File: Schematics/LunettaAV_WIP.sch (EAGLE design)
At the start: 97 parts, among them IC1 7809\, IC10 4051N, IC2 7805, IC3 4040N, IC4 TLC339P, IC5 4046N, IC6 4094N, IC7 40106N, IC8 4046N, IC9 4017N, J1 POWER_JACKPOWER_JACK_SLOT, J3 WQP-PJ301M-12_JACK, U1 LM358, U2 LM358, U3 MICROCHIP_MCP41050-I-PMICROCH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

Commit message: add more caps no cap
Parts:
- added C25: 10uF, SparkFun-Capacitors:10UF-POLAR-RADIAL-2.5MM-25V-20%
- added C26: 0.1uF, SparkFun-Capacitors:0.1UF-KIT-EZ-50V-20%
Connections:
- net 5V: now also C25.+, C26.1
- net GND: now also C25.-, C26.2
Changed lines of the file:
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@@
 <part name="C24" library="SparkFun-Capacitors" deviceset="10UF-POLAR" device="-RADIAL-2.5MM-25V-20%" value="10uF"/>
 <part name="D2" library="diode" library_urn="urn:adsk.eagle:library:210" deviceset="BAT42" device="" package3d_urn="urn:adsk.eagle:package:43344/2"/>
+<part name="C25" library="SparkFun-Capacitors" deviceset="10UF-POLAR" device="-RADIAL-2.5MM-25V-20%" value="10uF"/>
+<part name="C26" library="SparkFun-Capacitors" deviceset="0.1UF" device="-KIT-EZ-50V-20%" value="0.1uF"/>
 </parts>
 <sheets>
@@
 <attribute name="VALUE" x="298.069" y="-103.886" size="1.778" layer="96" rot="R90"/>
 </instance>
+<instance part="C25" gate="G$1" x="132.08" y="-294.64" smashed="yes">
+<attribute name="NAME" x="133.096" y="-294.005" size="1.778" layer="95" font="vector"/>
+<attribute name="VALUE" x="133.096" y="-298.831" size="1.778" layer="96" font="vector"/>
+</instance>
+<instance part="C26" gate="G$1" x="152.4" y="-302.26" smashed="yes">
+<attribute name="NAME" x="153.924" y="-299.339" size="1.778" layer="95" font="vector"/>
+<attribute name="VALUE" x="153.924" y="-304.419" size="1.778" layer="96" font="vector"/>
+</instance>
 </instances>
 <busses>
@@
 <label x="294.64" y="-109.22" size="1.778" layer="95"/>
 </segment>
+<segment>
+<pinref part="C25" gate="G$1" pin="-"/>
+<wire x1="132.08" y1="-299.72" x2="132.08" y2="-304.8" width="0.1524" layer="91"/>
+<label x="132.08" y="-312.42" size="1.778" layer="95"/>
+<pinref part="C26" gate="G$1" pin="2"/>
+<wire x1="132.08" y1="-304.8" x2="132.08" y2="-312.42" width="0.1524" layer="91"/>
+<wire x1="152.4" y1="-304.8" x2="132.08" y2="-304.8" width="0.1524" layer="91"/>
+<junction x="132.08" y="-304.8"/>
+</segment>
 </net>
 <net name="SR1" class="0">
@@
 <segment>
 <pinref part="U3" gate="G$0" pin="VDD"/>
-<wire x1="154.94" y1="-281.94" x2="142.24" y2="-281.94" width="0.1524" layer="91"/>
+<wire x1="154.94" y1="-281.94" x2="152.4" y2="-281.94" width="0.1524" layer="91"/>
 <label x="142.24" y="-281.94" size="1.778" layer="95"/>
-</segment>
-</net>
+<pinref part="C25" gate="G$1" pin="+"/>
+<wire x1="152.4" y1="-281.94" x2="149.86" y2="-281.94" width="0.1524" layer="91"/>
+<wire x1="149.86" y1="-281.94" x2="142.24" y2="-281.94" width="0.1524" layer="91"/>
+<wire x1="132.08" y1="-292.1" x2="132.08" y2="-287.02" width="0.1524" layer="91"/>
+<wire x1="132.08" y1="-287.02" x2="149.86" y2="-287.02" width="0.1524" layer="91"/>
+<wire x1="149.86" y1="-287.02" x2="149.86" y2="-281.94" width="0.1524" layer="91"/>
+<junction x="149.86" y="-281.94"/>
+<pinref part="C26" gate="G$1" pin="1"/>
+<wire x1="152.4" y1="-297.18" x2="152.4" y2="-281.94" width="0.1524" layer="91"/>
+<junction x="152.4" y="-281.94"/>
+</segment>
+</net>

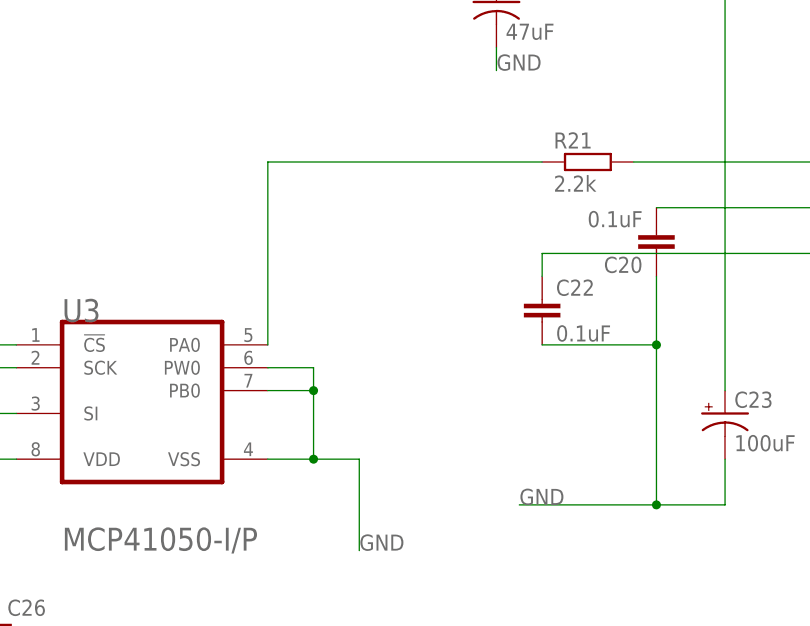
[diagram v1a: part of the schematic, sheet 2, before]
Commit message: code cleanups and parity among eagle and teensy naming schema
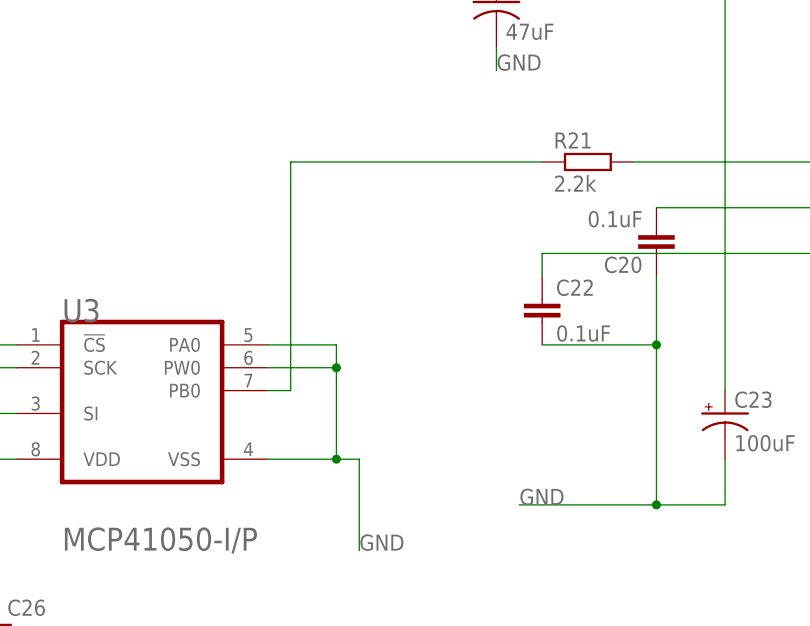
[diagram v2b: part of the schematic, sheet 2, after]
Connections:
- net ANALOGIN1 renamed DENSITYPIN
- net ANALOGIN2 renamed SPEEDPIN
- net DIN1 renamed BOUNCEPIN
- net GND: now also U3.PA0; no longer U3.PB0
- net N$33: now also U3.PB0; no longer U3.PA0
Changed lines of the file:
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@@
 </segment>
 </net>
-<net name="ANALOGIN1" class="0">
+<net name="DENSITYPIN" class="0">
 <segment>
 <pinref part="DENSITY" gate="G$1" pin="S"/>
@@
 </segment>
 </net>
-<net name="ANALOGIN2" class="0">
+<net name="SPEEDPIN" class="0">
 <segment>
 <pinref part="SPEED" gate="G$1" pin="S"/>
@@
 </segment>
 </net>
-<net name="DIN1" class="0">
+<net name="BOUNCEPIN" class="0">
 <segment>
 <label x="-33.02" y="91.44" size="1.778" layer="95"/>
@@
 </segment>
 <segment>
-<pinref part="U3" gate="G$0" pin="PW0"/>
-<wire x1="182.88" y1="-271.78" x2="187.96" y2="-271.78" width="0.1524" layer="91"/>
-<wire x1="187.96" y1="-271.78" x2="187.96" y2="-274.32" width="0.1524" layer="91"/>
-<pinref part="U3" gate="G$0" pin="PB0"/>
-<wire x1="187.96" y1="-274.32" x2="182.88" y2="-274.32" width="0.1524" layer="91"/>
 <pinref part="U3" gate="G$0" pin="VSS"/>
-<wire x1="182.88" y1="-281.94" x2="187.96" y2="-281.94" width="0.1524" layer="91"/>
-<wire x1="187.96" y1="-281.94" x2="193.04" y2="-281.94" width="0.1524" layer="91"/>
+<wire x1="182.88" y1="-281.94" x2="190.5" y2="-281.94" width="0.1524" layer="91"/>
+<wire x1="190.5" y1="-281.94" x2="193.04" y2="-281.94" width="0.1524" layer="91"/>
 <wire x1="193.04" y1="-281.94" x2="193.04" y2="-292.1" width="0.1524" layer="91"/>
 <label x="193.04" y="-292.1" size="1.778" layer="95"/>
-<wire x1="187.96" y1="-274.32" x2="187.96" y2="-281.94" width="0.1524" layer="91"/>
-<junction x="187.96" y="-274.32"/>
-<junction x="187.96" y="-281.94"/>
+<pinref part="U3" gate="G$0" pin="PA0"/>
+<wire x1="182.88" y1="-269.24" x2="190.5" y2="-269.24" width="0.1524" layer="91"/>
+<wire x1="190.5" y1="-269.24" x2="190.5" y2="-271.78" width="0.1524" layer="91"/>
+<pinref part="U3" gate="G$0" pin="PW0"/>
+<wire x1="190.5" y1="-271.78" x2="182.88" y2="-271.78" width="0.1524" layer="91"/>
+<wire x1="190.5" y1="-271.78" x2="190.5" y2="-281.94" width="0.1524" layer="91"/>
+<junction x="190.5" y="-271.78"/>
+<junction x="190.5" y="-281.94"/>
 </segment>
 <segment>
@@
 <net name="N$33" class="0">
 <segment>
-<pinref part="U3" gate="G$0" pin="PA0"/>
-<wire x1="182.88" y1="-269.24" x2="182.88" y2="-248.92" width="0.1524" layer="91"/>
 <pinref part="R21" gate="G$1" pin="1"/>
-<wire x1="182.88" y1="-248.92" x2="213.36" y2="-248.92" width="0.1524" layer="91"/>
-</segment>
-</net>
+<pinref part="U3" gate="G$0" pin="PB0"/>
+<wire x1="185.42" y1="-248.92" x2="213.36" y2="-248.92" width="0.1524" layer="91"/>
+<wire x1="182.88" y1="-274.32" x2="185.42" y2="-274.32" width="0.1524" layer="91"/>
+<wire x1="185.42" y1="-274.32" x2="185.42" y2="-248.92" width="0.1524" layer="91"/>
+</segment>
+</net>

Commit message: brd init
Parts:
- removed J2: (no value), SparkFun-Connectors:CONN_04LONGPADS
- added JP6: (no value), pinhead:PINHD-2X8
- C10, C15, C26, C7, C9: value 0.1uF -> 10uF; device SparkFun-Capacitors:0.1UF-KIT-EZ-50V-20% -> SparkFun-Capacitors:10UF-POLAR-RADIAL-2.5MM-25V-20%
- C14: value .1uF -> 0.1uF; device capacitor-wima:C2.5/2 -> SparkFun-Capacitors:0.1UF-KIT-EZ-50V-20%
- C18: value 47uF -> 0.1uF; device SparkFun-Capacitors:10UF-POLAR-RADIAL-2.5MM-25V-20% -> SparkFun-Capacitors:0.1UF-KIT-EZ-50V-20%
- C19: value 0.1uF -> .1uF; device SparkFun-Capacitors:0.1UF-KIT-EZ-50V-20% -> capacitor-wima:C2.5/2
- C2, C24, C25, C3, C5: value 10uF -> 0.1uF; device SparkFun-Capacitors:10UF-POLAR-RADIAL-2.5MM-25V-20% -> SparkFun-Capacitors:0.1UF-KIT-EZ-50V-20%
- C20: value 0.1uF -> 47uF; device SparkFun-Capacitors:0.1UF-KIT-EZ-50V-20% -> SparkFun-Capacitors:10UF-POLAR-RADIAL-2.5MM-25V-20%
- FDBK, MIX: value (none) -> 100k
- IC1: value 7809\ -> TLC339P; device v-reg:78XXS -> linear:TLC339P
- IC10: value 4051N -> 40106N; device 40xx:4051N -> 40xx:40106N
- IC2: value 7805 -> 4046N; device v-reg:78XXS -> 40xx:4046N
- IC3: value 4040N -> 7809\; device 40xx:4040N -> v-reg:78XXS
- IC4: value TLC339P -> 4040N; device linear:TLC339P -> 40xx:4040N
- IC5: value 4046N -> 7805; device 40xx:4046N -> v-reg:78XXS
- IC6: value 4094N -> 4017N; device 40xx:4094N -> 40xx:4017N
- IC7: value 40106N -> 4051N; device 40xx:40106N -> 40xx:4051N
- IC8: value 4046N -> 4094N; device 40xx:4046N -> 40xx:4094N
- IC9: value 4017N -> 4046N; device 40xx:4017N -> 40xx:4046N
- JP1: device pinhead:PINHD-1X2 -> jumper:JP4E
- JP2: device adafruit:PINHD-2X4 -> pinhead:PINHD-1X2
- JP4: device pinhead:PINHD-2X8 -> adafruit:PINHD-2X4
- R1, R2: value 4.7K -> 10K
- R10: value 10K -> 4.7k
- R12: value 100K -> 4.7k
- R13, R3: value 1K -> 10K
- R14: value 1K -> 4.7k
- R15: value LDR -> 100K; device rcl:R-EU_0204/2V -> MusicThingModular:RESISTOR7MM
- R17, R29: value 10k -> 100k
- R18: value 10K -> 10k
- R19, R20: value 10K -> 100k
- R21: value 2.2k -> 10k
- R22: value 100k -> 1K
- R23: value 100k -> 10K
- R24, R25: value 4.7k -> 10K
- R26: value 4.7k -> 1K
- R28: value 100k -> LDR; device MusicThingModular:RESISTOR7MM -> rcl:R-EU_0204/2V
- R30: value 100k -> 2.2k
- R5, R9: value 10K -> 4.7K
- R6: value 10K -> 1K
- U2: value LM358 -> MICROCHIP_MCP41050-I-PMICROCHIP_MCP41050-I-P_0_0; device SparkFun-IC-Amplifiers:LM358 -> MCP41050:MICROCHIP_MCP41050-I-PMICROCHIP_MCP41050-I-P_0_0
- U3: value MICROCHIP_MCP41050-I-PMICROCHIP_MCP41050-I-P_0_0 -> LM358; device MCP41050:MICROCHIP_MCP41050-I-PMICROCHIP_MCP41050-I-P_0_0 -> SparkFun-IC-Amplifiers:LM358
- renumbered CLOCK-OUT to CLOCKOUT, FDBCK to FDBK, J3 to OUTPUT, PITCH to FREQ, S1 to PATTERNOFFSET, S2 to WRITE, S3 to ERASE, VR1 to VR4
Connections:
- net 3V3: now also C2.1, C3.1, R11.2, R13.2, R9.2; no longer C1.1, C4.1, R1.2, R2.2, R6.2
- net 5V: now also C10.+, C15.+, C16.1, IC1A.-IN, IC1B.-IN, IC1C.-IN, IC1D.-IN, IC5.OUT, JP2.1, R10.2, R12.2, R14.2, U2.VDD; no longer C25.+, C26.1, C5.+, IC2.OUT, IC4A.-IN, IC4B.-IN, IC4C.-IN, IC4D.-IN, JP1.1, R24.2, R25.2, R26.2, U3.VDD
- net 9V: now also C1.1, C14.1, C18.1, C4.1, C5.1, C9.+, IC10P.VDD, IC1P.V+, IC2P.VDD, IC3.OUT, IC4P.VDD, IC5.IN, IC7P.VCC, IC8A.OE, IC8A.STR, R22.1, U3G3.P$V+; no longer C15.1, C16.1, C3.+, C6.1, C7.1, C9.1, IC1.OUT, IC10P.VCC, IC2.IN, IC3P.VDD, IC4P.V+, IC5P.VDD, IC6A.OE, IC6A.STR, IC7P.VDD, R13.1, U2G3.P$V+
- net AUDIORATE: now also IC10C.O, IC6A.CLK; no longer IC7C.O, IC9A.CLK
- net BOUNCEPIN: now also R6.2; no longer R3.2
- net BUFFCLOCK: now also IC8A.CLK, R16.1; no longer IC6A.CLK, R22.1
- net BUFFMEL: now also R31.1, U3G2.-IN, U3G2.OUT; no longer R16.1, U2G2.-IN, U2G2.OUT
- net CLOCKSELECT: now also JP4.2, JP4.4, JP4.6, JP4.8; no longer JP2.2, JP2.4, JP2.6, JP2.8
- net DCIN: now also C7.+, IC3.IN; no longer C2.+, IC1.IN
- net DPOTDATA: now also R12.1, U2.SI; no longer R25.1, U3.SI
- net DPOTSCK: now also R14.1, U2.SCK; no longer R26.1, U3.SCK
- net DPOTSEL: now also R10.1, U2.!CS!; no longer R24.1, U3.!CS!
- net GND: now also C10.-, C15.-, C18.2, C19.2, C2.2, C20.-, C21.2, C22.1, C24.1, C3.2, C5.2, C7.-, C9.-, IC10D.I, IC10E.I, IC10F.I, IC10P.VSS, IC1P.V-, IC2A.INH, IC2P.VSS, IC3.GND, IC4P.VSS, IC5.GND, IC6A.ENA, IC7A.INH, IC7P.GND, IC7P.VEE, J1.GNDBREAK, R1.1, R15.1, R17.1, R2.1, R23.1, R24.1, R25.1, R29.2, R6.1, U2.PA0, U2.PW0, U2.VSS, U3G3.P$V-; no longer C15.2, C18.-, C19.1, C2.-, C20.1, C22.2, C25.-, C26.2, C3.-, C5.-, C6.2, C7.2, C9.2, IC1.GND, IC10A.INH, IC10P.GND, IC10P.VEE, IC2.GND, IC3P.VSS, IC4P.V-, IC5A.INH, IC5P.VSS, IC7D.I, IC7E.I, IC7F.I, IC7P.VSS, IC9A.ENA, R10.1, R11.1, R12.1, R18.1, R19.1, R23.2, R28.1, R31.1, R9.1, U2G3.P$V-, U3.PA0, U3.PW0, U3.VSS
- net LDRIVER: now also R19.1; no longer R30.1
- net MELODYOUT: now also IC6A.Q0, U3G2.+IN; no longer IC9A.Q0, U2G2.+IN
- net MOOX: now also IC7A.C, R25.2; no longer IC10A.C, R20.2
- net MOXO: now also IC7A.B, R24.2; no longer IC10A.B, R19.2
- net MXOO: now also IC7A.A, R23.2; no longer IC10A.A, R18.2
- net N$1: now also JP2.2; no longer JP1.2
- net N$10: now also IC10B.O, IC10C.I; no longer IC7B.O, IC7C.I
- net N$11: now also C19.1, IC10A.I, R28.2; no longer C14.1, IC7A.I, R15.2
- net N$12: now also C25.1; no longer C21.1
- net N$13: now also R27.2, R29.1, U3G1.+IN; no longer R22.2, R23.1, U2G1.+IN
- net N$14: now also U3G1.-IN, U3G1.OUT; no longer U2G1.-IN, U2G1.OUT
- net N$15: now also R30.2; no longer R21.2
- net N$16: now also C20.+; no longer C18.+
- net N$17: now also C22.2; no longer C20.2
- net N$18: now also C21.1; no longer C22.1
- net N$19: now also IC6A.RES, IC7A.X; no longer IC10A.X, IC9A.RES
- net N$2: now also C6.2, IC2A.CX@2; no longer C10.2, IC5A.CX@2
- net N$20: now also IC6A.Q2, IC7A.X0; no longer IC10A.X0, IC9A.Q2
- net N$21: now also IC6A.Q3, IC7A.X1; no longer IC10A.X1, IC9A.Q3
- net N$22: now also IC6A.Q4, IC7A.X2; no longer IC10A.X2, IC9A.Q4
- net N$23: now also IC6A.Q5, IC7A.X3; no longer IC10A.X3, IC9A.Q5
- net N$24: now also IC6A.Q6, IC7A.X4; no longer IC10A.X4, IC9A.Q6
- net N$25: now also IC6A.Q7, IC7A.X5; no longer IC10A.X5, IC9A.Q7
- net N$26: now also IC6A.Q8, IC7A.X6; no longer IC10A.X6, IC9A.Q8
- net N$27: now also IC6A.Q9, IC7A.X7; no longer IC10A.X7, IC9A.Q9
- net N$28: now also IC8A.D, R26.1; no longer IC6A.D, R14.1
- net N$29: now also R31.2, R32.1; no longer R16.2, R17.1
- net N$3: now also R5.1; no longer R1.1
- net N$30: now also R32.2; no longer R17.2
- net N$31: now also C24.2; no longer C19.2
- net N$33: now also R30.1, U2.PB0; no longer R21.1, U3.PB0
- net N$34: now also R16.2, R17.2; no longer R27.2, R28.2
- net N$35: now also R18.1; no longer R29.1
- net N$36: now also R18.2; no longer R29.2
- net N$37: now also R19.2, R20.2; no longer R30.2, R31.2
- net N$38: now also R21.1; no longer R32.1
- net N$39: now also R21.2; no longer R32.2
- net N$4: now also R9.1; no longer R2.1
- net N$41: now also C26.-; no longer C24.-
- net N$5: now also C6.1, IC2A.CX@1; no longer C10.1, IC5A.CX@1
- net N$6: now also IC2A.R1, R15.2; no longer IC5A.R1, R12.2
- net N$7: now also C25.2; no longer C21.2
- net N$8: now also R22.2; no longer R13.2
- net N$9: now also IC10A.O, IC10B.I, R28.1; no longer IC7A.O, IC7B.I, R15.1
- net OOX: now also IC1D.+IN, JP1.4, R8.2; no longer IC4D.+IN, J2.4, R11.2
- net OUT: now also C26.+; no longer C24.+
- net OXO: now also IC1C.+IN, JP1.3, R3.2; no longer IC4C.+IN, J2.3, R10.2
- net PLL/16: now also IC4A.Q4; no longer IC3A.Q4
- net PLL/2: now also IC4A.Q1, JP4.3; no longer IC3A.Q1, JP2.3
- net PLL/32: now also IC4A.Q5; no longer IC3A.Q5
- net PLL/4: now also IC4A.Q2, JP4.5; no longer IC3A.Q2, JP2.5
- net PLL/8: now also IC4A.Q3, JP4.7; no longer IC3A.Q3, JP2.7
- net PLLCLOCKOUT: now also IC2A.VCOOUT, IC4A.P1, JP4.1; no longer IC3A.P1, IC5A.VCOOUT, JP2.1
- net RESET: now also IC1A.+IN, JP1.1, R1.2; no longer IC4A.+IN, J2.1, R8.2
- net SPEEDYBUFF: now also IC2A.VCOIN; no longer IC5A.VCOIN
- net SR1: now also IC8A.Q1, JP6.1, JP6.2; no longer IC6A.Q1, JP4.1, JP4.2
- net SR2: now also IC8A.Q2, JP6.3, JP6.4; no longer IC6A.Q2, JP4.3, JP4.4
- net SR3: now also IC8A.Q3, JP6.5, JP6.6; no longer IC6A.Q3, JP4.5, JP4.6
- net SR4: now also IC8A.Q4, JP6.7, JP6.8; no longer IC6A.Q4, JP4.7, JP4.8
- net SR5: now also IC8A.Q5, JP6.10, JP6.9; no longer IC6A.Q5, JP4.10, JP4.9
- net SR6: now also IC8A.Q6, JP6.11, JP6.12; no longer IC6A.Q6, JP4.11, JP4.12
- net SR7: now also IC8A.Q7, JP6.13, JP6.14; no longer IC6A.Q7, JP4.13, JP4.14
- net SR8: now also IC8A.Q8, JP6.15, JP6.16, R26.2; no longer IC6A.Q8, JP4.15, JP4.16, R14.2
- net TNSYOOX: now also IC1D.OUT, R13.1; no longer IC4D.OUT, R7.1
- net TNSYOXO: now also IC1C.OUT, R11.1; no longer IC4C.OUT, R6.1
- net TNSYRES: now also IC1A.OUT; no longer IC4A.OUT
- net TNSYXOO: now also IC1B.OUT, R7.1; no longer IC4B.OUT, R5.1
- net XOO: now also IC1B.+IN, JP1.2, R2.2; no longer IC4B.+IN, J2.2, R9.2
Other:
- moved on the sheet: C1, C11, C13, C14, C16, C17, C19, C21, C22, C4, C6, IC6P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

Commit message: PCB Design
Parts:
- removed IC9: 4046N, 40xx:4046N
- removed LED1, LED2: (no value), led:LED3MM
- added CLOCK, MS4: (no value), SparkFun-LED:LED3MM
- C14: value 0.1uF -> 10uF; device SparkFun-Capacitors:0.1UF-KIT-EZ-50V-20% -> SparkFun-Capacitors:10UF-POLAR-RADIAL-2.5MM-25V-20%
- renumbered DD1 to PT2399, JP1 to TNSYSELECT, JP2 to TNSYPWR, JP3 to CLOCKDIV, JP5 to MUXSELECT, JP6 to SHIFTREG, U2 to MCP41050
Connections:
- net 3V3: now also B1.3V, C14.+
- net 9V: now also CLOCK.A, MS4.A; no longer C14.1, IC9P.VDD, LED1.A, LED2.A
- net GND: now also C14.-; no longer C14.2, IC9P.VSS
- net N$36: now also CLOCK.C; no longer LED1.C
- net N$39: now also MS4.C; no longer LED2.C

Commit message: redo routing
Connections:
- net N$3 renamed SCL
- net N$4 renamed SDA
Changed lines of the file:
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@@
 </class>
 <class number="1" name="POWER" width="0.635" drill="0">
+<clearance class="1" value="0.508"/>
+</class>
+<class number="2" name="COMMS" width="0.635" drill="0">
+<clearance class="2" value="0.508"/>
 </class>
 </classes>
@@
 </segment>
 </net>
-<net name="N$3" class="0">
+<net name="SCL" class="2">
 <segment>
 <pinref part="B1" gate="G$1" pin="A5/19/SCL0"/>
@@
 <pinref part="OL96$1" gate="G$1" pin="SCL"/>
 <wire x1="-2.54" y1="147.32" x2="5.08" y2="147.32" width="0.1524" layer="91"/>
-</segment>
-</net>
-<net name="N$4" class="0">
+<label x="-22.86" y="121.92" size="1.778" layer="95"/>
+</segment>
+</net>
+<net name="SDA" class="2">
 <segment>
 <pinref part="B1" gate="G$1" pin="A4/18/SDA0"/>
@@
 <wire x1="-25.4" y1="119.38" x2="0" y2="119.38" width="0.1524" layer="91"/>
 <junction x="0" y="119.38"/>
+<label x="-22.86" y="119.38" size="1.778" layer="95"/>
 </segment>
 </net>
@@
 </segment>
 </net>
-<net name="DPOTSCK" class="0">
+<net name="DPOTSCK" class="2">
 <segment>
 <pinref part="B1" gate="G$1" pin="13/SCK"/>
@@
 </segment>
 </net>
-<net name="DPOTDATA" class="0">
+<net name="DPOTDATA" class="2">
 <segment>
 <pinref part="B1" gate="G$1" pin="11/DOUT"/>
@@
 </segment>
 </net>
-<net name="DPOTSEL" class="0">
+<net name="DPOTSEL" class="2">
 <segment>
 <pinref part="B1" gate="G$1" pin="10*/TX2/CS"/>
@@
 </segment>
 </net>
-<net name="DPOTSEL" class="0">
+<net name="DPOTSEL" class="2">
 <segment>
 <pinref part="MCP41050" gate="G$0" pin="!CS!"/>
@@
 </segment>
 </net>
-<net name="DPOTSCK" class="0">
+<net name="DPOTSCK" class="2">
 <segment>
 <pinref part="MCP41050" gate="G$0" pin="SCK"/>
@@
 </segment>
 </net>
-<net name="DPOTDATA" class="0">
+<net name="DPOTDATA" class="2">
 <segment>
 <pinref part="MCP41050" gate="G$0" pin="SI"/>
